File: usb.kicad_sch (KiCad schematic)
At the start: 57 parts, among them J901 AU-Y1008-2-BLK, J902 AU-Y1008-2-BLK, U901 USB2514B/M2, U902 AP22966DC8-7, U903 AP22966DC8-7, Y901 24 MHz

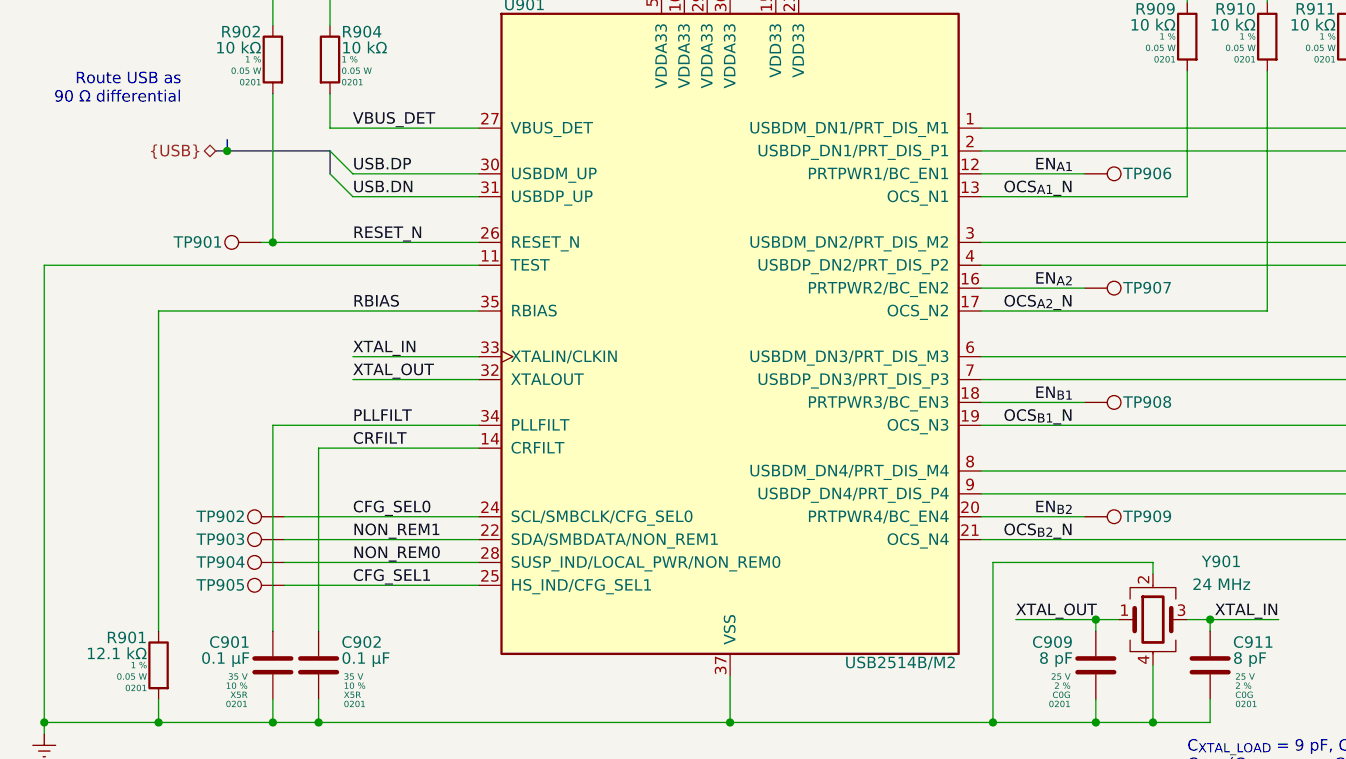
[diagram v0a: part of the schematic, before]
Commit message: Remove redundant test points
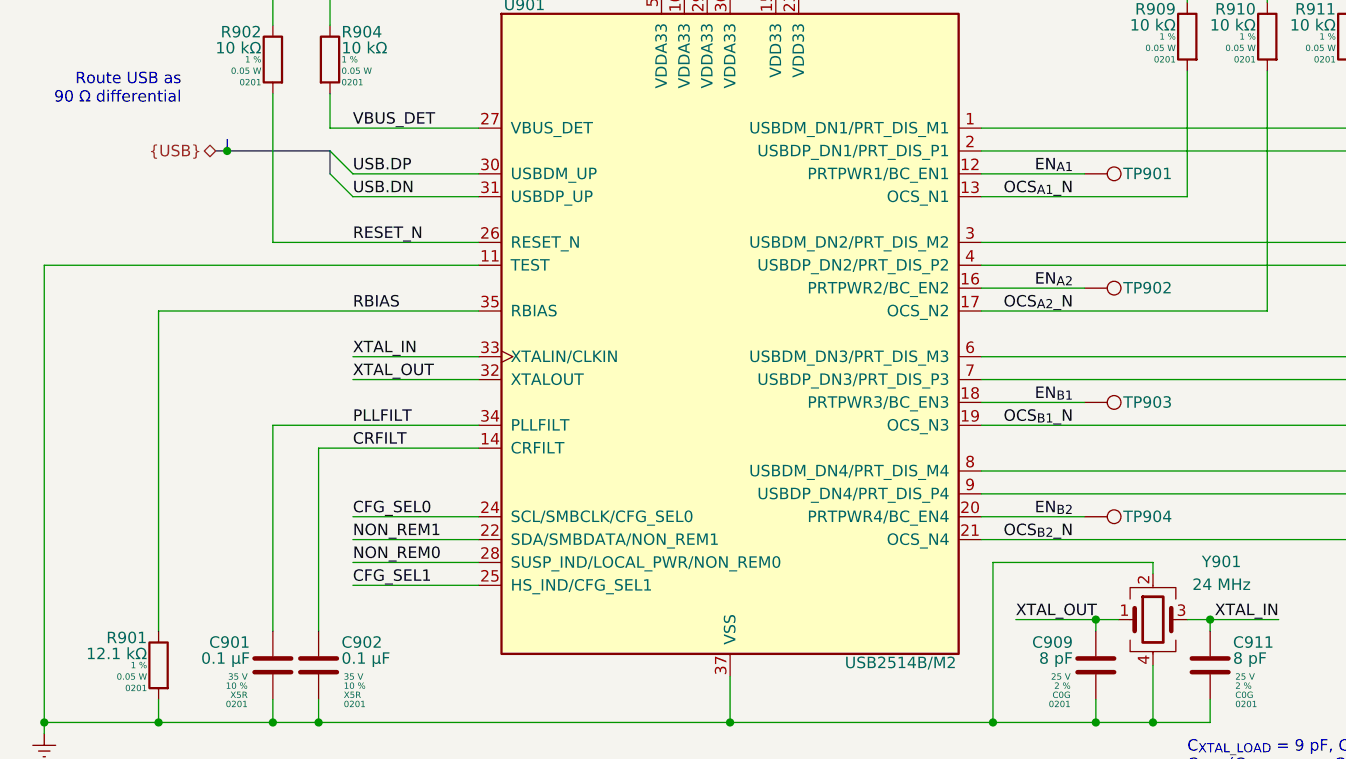
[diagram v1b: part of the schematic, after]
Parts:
- removed TP901, TP902, TP903, TP904, TP905: TestPoint, TestPoint:TestPoint_Pad_D1.0mm, symbol Connector:TestPoint
- renumbered TP906 to TP901, TP907 to TP902, TP908 to TP903, TP909 to TP904

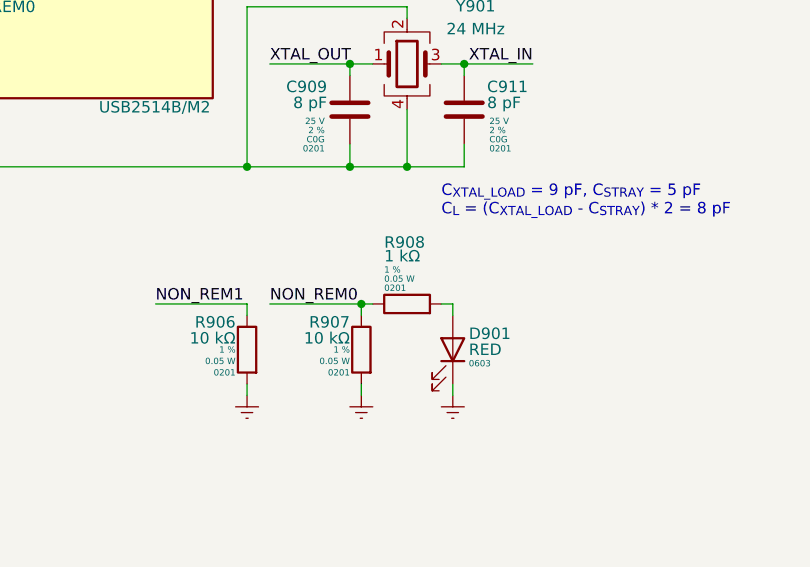
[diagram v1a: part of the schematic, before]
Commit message: Decrease LED brightness
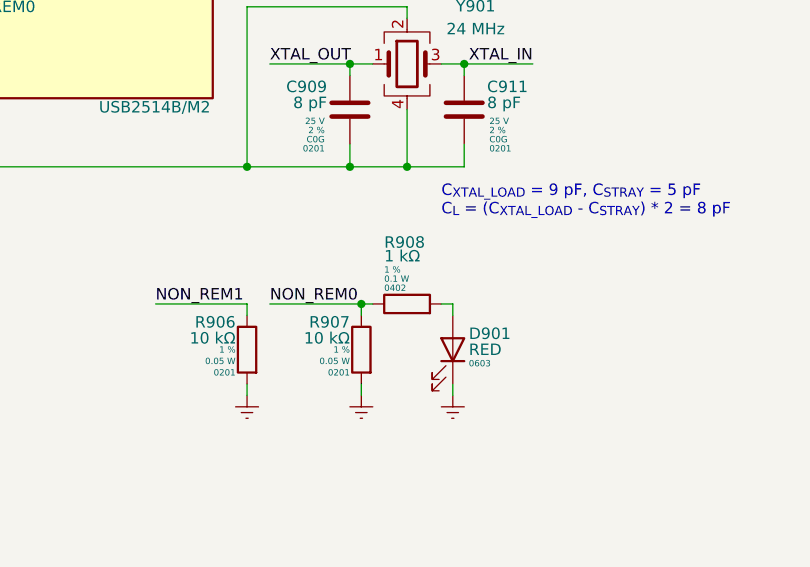
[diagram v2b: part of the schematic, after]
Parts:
- R908: footprint perfect_footprints:R_0201_0603Metric -> perfect_footprints:R_0402_1005Metric_HDI; Digi-Key Part Number 10-ERJ-U01F1001CCT-ND -> P1.00KLCT-ND; MPN ERJ-U01F1001C -> ERJ-2RKF1001X; Power rating 0.05 W -> 0.1 W; Size 0201 -> 0402
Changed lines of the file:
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@@
 			)
 		)
-		(property "Footprint" "perfect_footprints:R_0201_0603Metric"
+		(property "Footprint" "perfect_footprints:R_0402_1005Metric_HDI"
 			(at 148.59 204.978 90)
 			(effects
@@
 			)
 		)
-		(property "Datasheet" "https://industrial.panasonic.com/cdbs/www-data/pdf/RDP0000/AOA0000C334.pdf"
+		(property "Datasheet" "https://industrial.panasonic.com/cdbs/www-data/pdf/RDA0000/AOA0000C304.pdf"
 			(at 148.59 203.2 0)
 			(effects
@@
 			)
 		)
-		(property "Description" "1 kOhms ±1% 0.05W, 1/20W Chip Resistor 0201 (0603 Metric) Anti-Sulfur Thick Film"
+		(property "Description" "1 kOhms ±1% 0.1W, 1/10W Chip Resistor 0402 (1005 Metric) Automotive AEC-Q200 Thick Film"
 			(at 148.59 203.2 0)
 			(effects
@@
 			)
 		)
-		(property "MPN" "ERJ-U01F1001C"
+		(property "MPN" "ERJ-2RKF1001X"
 			(at 148.59 203.2 0)
 			(effects
@@
 			)
 		)
-		(property "Power rating" "0.05 W"
+		(property "Power rating" "0.1 W"
 			(at 146.05 200.406 90)
 			(effects
@@
 			)
 		)
-		(property "Size" "0201"
+		(property "Size" "0402"
 			(at 146.05 201.422 90)
 			(effects
@@
 			)
 		)
-		(property "Digi-Key Part Number" "10-ERJ-U01F1001CCT-ND"
+		(property "Digi-Key Part Number" "P1.00KLCT-ND"
 			(at 148.59 203.2 90)
 			(effects

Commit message: Refactor passives
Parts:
- C903, C912, C913, C914, C915: footprint Capacitor_SMD:C_0603_1608Metric -> perfect_footprints:C_0402_1005Metric_HDI; Digi-Key Part Number 490-7205-1-ND -> 1276-6836-1-ND; MPN GRM188R6YA475KE15D -> CL05A475MO5NUNC; Manufacturer Murata Electronics -> Samsung Electro-Mechanics; Size 0603 -> 0402; Voltage rating 35 V -> 16 V
- C916, C917, C918, C919: value 1000 pF -> 3300 pF; footprint perfect_footprints:C_0201_0603Metric -> perfect_footprints:C_0402_1005Metric_HDI; Digi-Key Part Number 490-3184-1-ND -> 490-GCM155R71H332KA37JCT-ND; MPN GRM033R71E102KA01D -> GCM155R71H332KA37J; Size 0201 -> 0402; Voltage rating 25 V -> 50 V
- renumbered C910 to C909, C909 to C910
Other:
- moved on the sheet: C904, C905, C906, C907, C908, C909

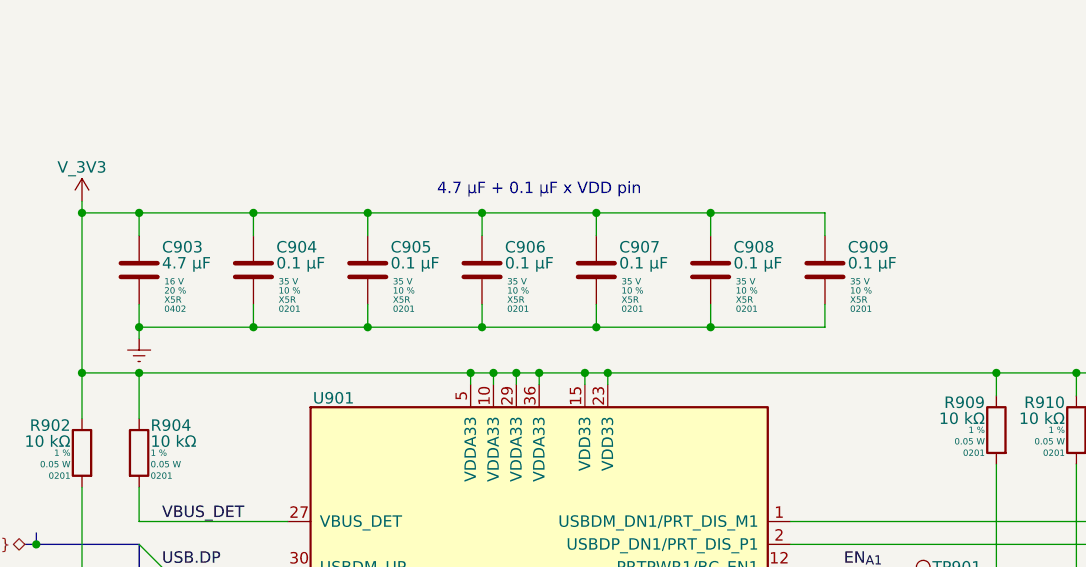
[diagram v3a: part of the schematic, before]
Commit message: Refactor decoupling caps
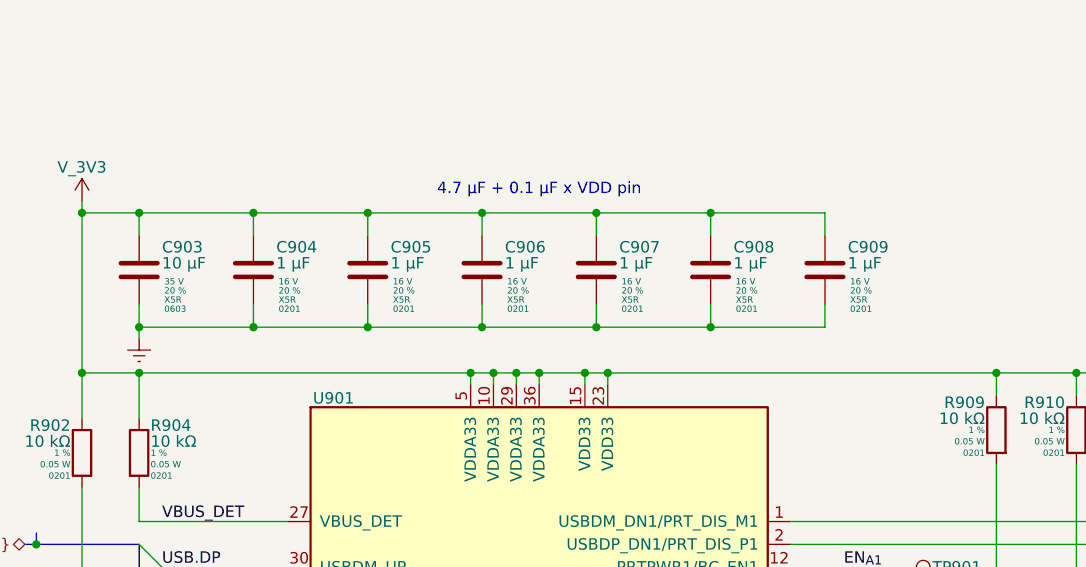
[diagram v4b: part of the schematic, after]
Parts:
- C903: value 4.7 µF -> 10 µF; footprint perfect_footprints:C_0402_1005Metric_HDI -> Capacitor_SMD:C_0603_1608Metric; Digi-Key Part Number 1276-6836-1-ND -> 490-13248-1-ND; MPN CL05A475MO5NUNC -> GRM188R6YA106MA73D; Manufacturer Samsung Electro-Mechanics -> Murata Electronics; Size 0402 -> 0603; Voltage rating 16 V -> 35 V
- C904, C905, C906, C907, C908, C909: value 0.1 µF -> 1 µF; Digi-Key Part Number 490-10430-1-ND -> 490-18654-1-ND; MPN GRM033R6YA104KE14D -> GRM033R61C105ME15D; Tolerance 10 % -> 20 %; Voltage rating 35 V -> 16 V

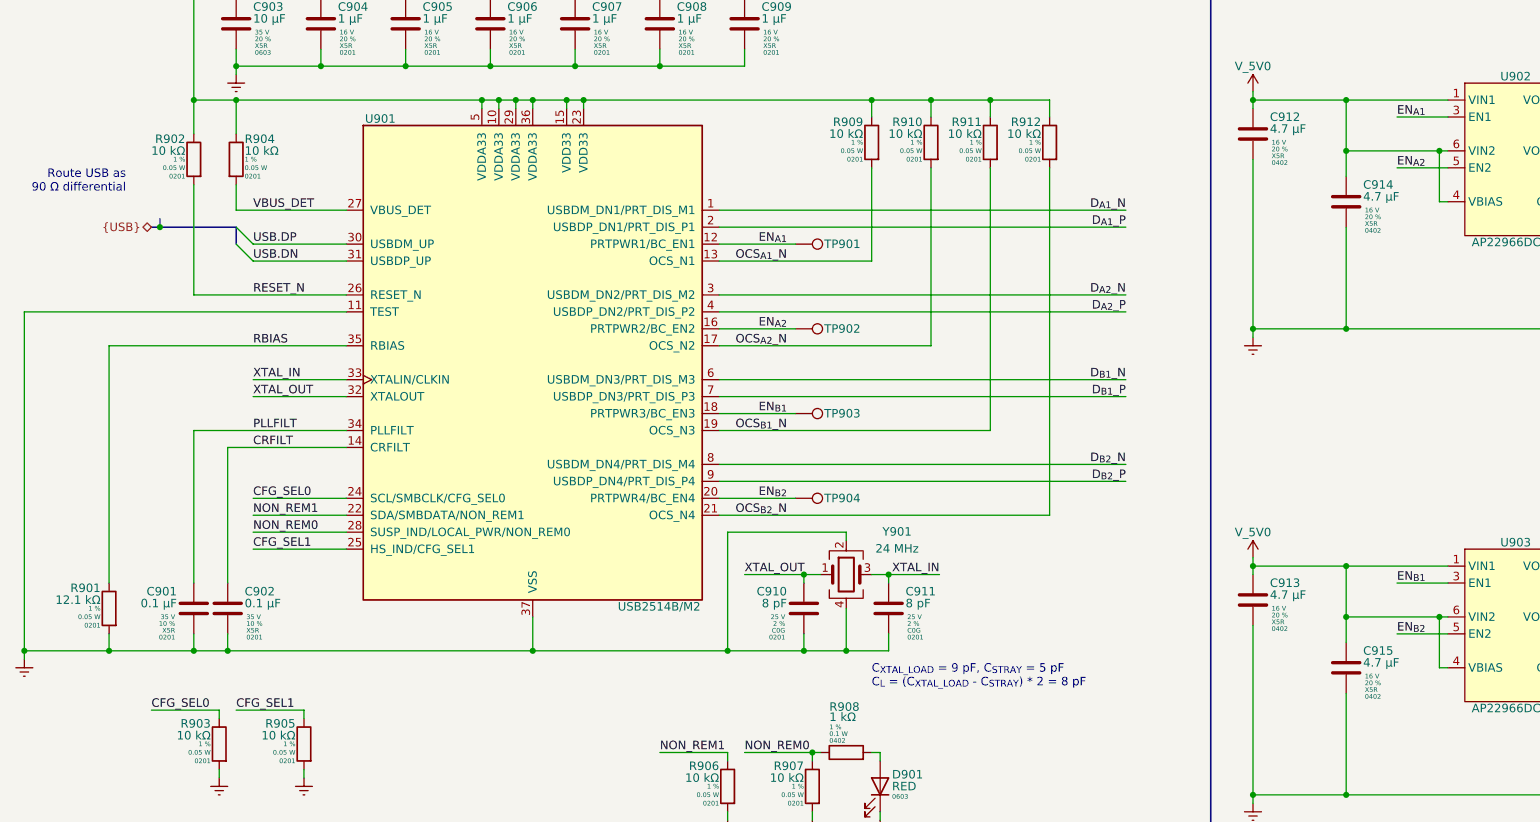
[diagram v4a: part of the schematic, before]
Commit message: Refactor more decoupling caps
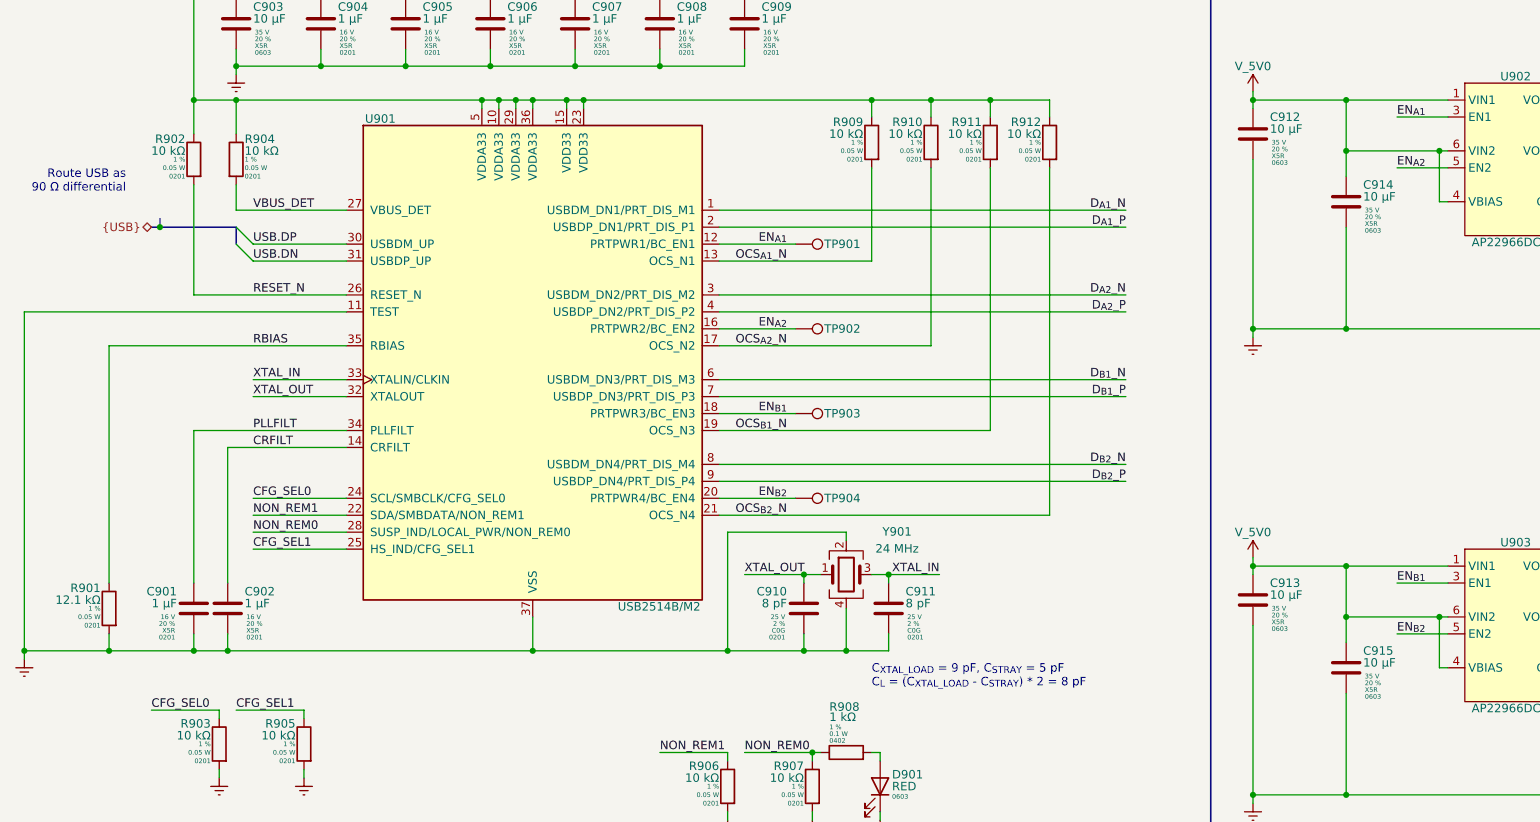
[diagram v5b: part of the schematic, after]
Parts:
- C901, C902: value 0.1 µF -> 1 µF; Digi-Key Part Number 490-10430-1-ND -> 490-18654-1-ND; MPN GRM033R6YA104KE14D -> GRM033R61C105ME15D; Tolerance 10 % -> 20 %; Voltage rating 35 V -> 16 V
- C912, C913, C914, C915: value 4.7 µF -> 10 µF; footprint perfect_footprints:C_0402_1005Metric_HDI -> Capacitor_SMD:C_0603_1608Metric; Digi-Key Part Number 1276-6836-1-ND -> 490-13248-1-ND; MPN CL05A475MO5NUNC -> GRM188R6YA106MA73D; Manufacturer Samsung Electro-Mechanics -> Murata Electronics; Size 0402 -> 0603; Voltage rating 16 V -> 35 V
